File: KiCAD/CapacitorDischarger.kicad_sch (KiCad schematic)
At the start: 47 parts, among them J1 SLB4-G-21, J2 SLB4-G-22, J3 MKDS5/2-9.5, J4 MKDS5/2-9.5, J5 PM-128 input, Q1 MPSA42, Q2 STP10NK80Z

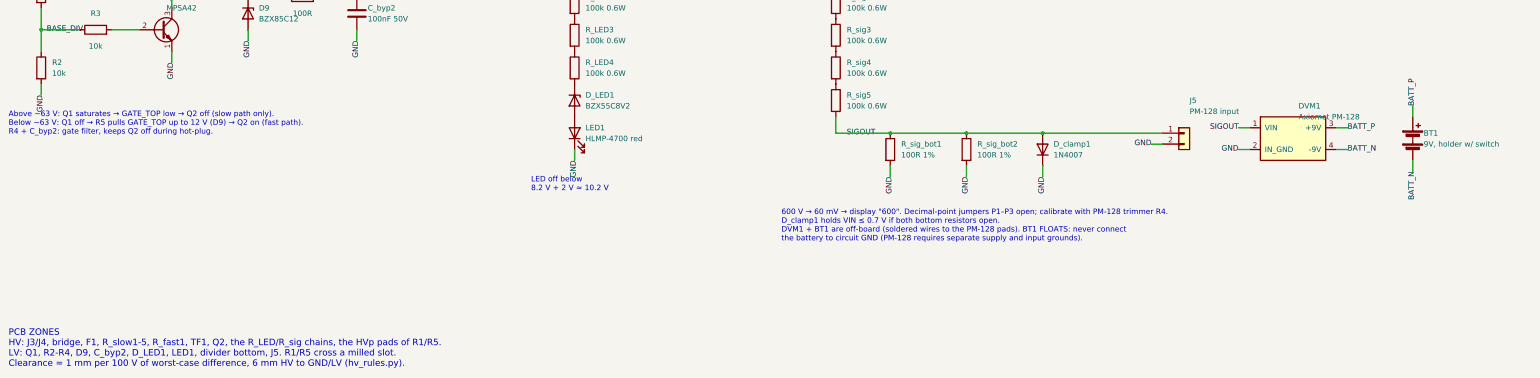
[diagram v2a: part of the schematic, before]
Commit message: Enclosure, front-panel LED via XH, DC-jack 9 V supply, build instructions
- mechanical/enclosure: parametric FreeCAD case for the single-sided board
  (base + screwed cover, PM-128 in the cover, sockets in line with J3/J4,
  9 V jack on the left wall with a floating-supply warning, LED on the front,
  baffled vents, snap hooks + supports for the 2-hole PCB), fit-check script
- LED1 off-board on a JST XH cable (J6); D_clamp2 (BZX55C8V2) holds LED_A at
  8.2 V if the LED is unplugged; sims 15/15 PASS; both boards re-placed, DRC clean
- PM-128 powered from any floating 9 V via a panel DC jack (battery box dropped)
- instruction.md: PCB making, assembly, wiring, tests, calibration, use

Co-Authored-By: Claude Opus 5.5 (1M context) <noreply@anthropic.com>
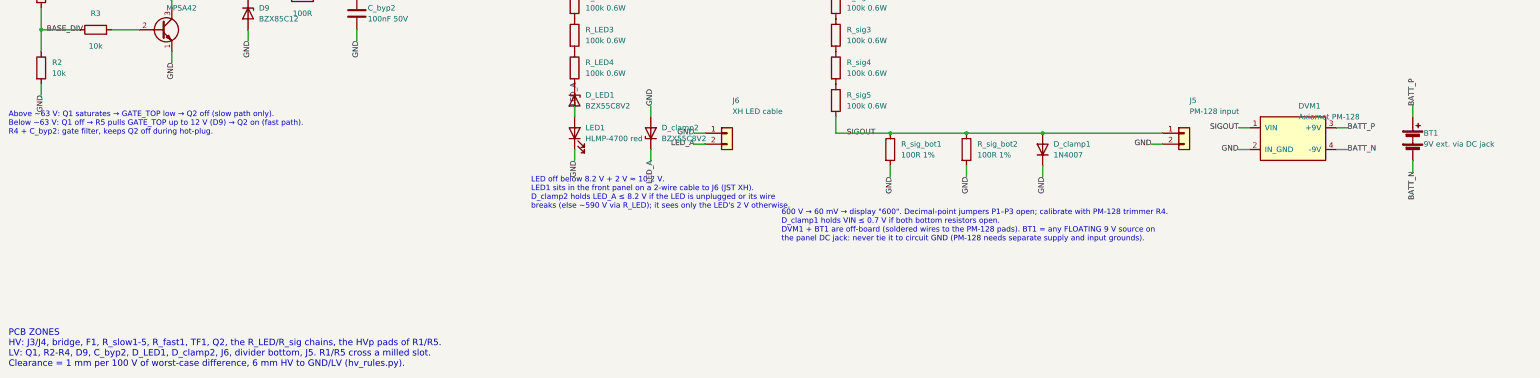
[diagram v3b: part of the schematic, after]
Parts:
- added D_clamp2: BZX55C8V2, Diode_THT:D_DO-35_SOD27_P5.08mm_Vertical_AnodeUp, symbol Device:D_Zener
- added J6: XH LED cable, Connector_JST:JST_XH_B2B-XH-A_1x02_P2.50mm_Vertical, symbol Connector_Generic:Conn_01x02
- BT1: value 9V, holder w/ switch -> 9V ext. via DC jack; MPN Westinghouse 6LR61 + 9 V battery box with ON/OFF switch (bo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 -> Mufa DC mama 5.5x2.1 (ComponentsDB comp_231, same jack as S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
- LED1: footprint LED_THT:LED_D5.0mm -> (none)
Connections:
- net GND: now also D_clamp2.2 (A), J6.1 (Pin_1)
- net LED_A: now reaches D_LED1.2 (A), LED1.2 (A)
- net LED_A: now also D_clamp2.1 (K), J6.2 (Pin_2)
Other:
- note added: "600 V → 60 mV → display "600". Decimal-point jumpers P1–P3 open; calibrate with PM-128 trimmer R4. D_clamp1 holds VIN ≤ 0.7 V if both bottom resistors open. DVM1 + BT1 are off-board (soldered wires to the PM-128 pads). BT1 = any FLOATING 9 V source on the panel DC jack: never tie it to circuit GND (PM-128 needs separate supply and input grounds)."
- note added: "LED off below 8.2 V + 2 V ≈ 10.2 V. LED1 sits in the front panel on a 2-wire cable to J6 (JST XH). D_clamp2 holds LED_A ≤ 8.2 V if the LED is unplugged or its wire breaks (else ~590 V via R_LED); it sees only the LED's 2 V otherwise."
- note added: "PCB ZONES HV: J3/J4, bridge, F1, R_slow1-5, R_fast1, TF1, Q2, the R_LED/R_sig chains, the HVp pads of R1/R5. LV: Q1, R2-R4, D9, C_byp2, D_LED1, D_clamp2, J6, divider bottom, J5. R1/R5 cross a milled slot. Clearance = 1 mm per 100 V of worst-case difference, 6 mm HV to GND/LV (hv_rules.py)."
- note removed: "600 V → 60 mV → display "600". Decimal-point jumpers P1–P3 open; calibrate with PM-128 trimmer R4. D_clamp1 holds VIN ≤ 0.7 V if both bottom resistors open. DVM1 + BT1 are off-board (soldered wires to the PM-128 pads). BT1 FLOATS: never connect the battery to circuit GND (PM-128 requires separate supply and input grounds)."
- note removed: "LED off below 8.2 V + 2 V ≈ 10.2 V"
- note removed: "PCB ZONES HV: J3/J4, bridge, F1, R_slow1-5, R_fast1, TF1, Q2, the R_LED/R_sig chains, the HVp pads of R1/R5. LV: Q1, R2-R4, D9, C_byp2, D_LED1, LED1, divider bottom, J5. R1/R5 cross a milled slot. Clearance = 1 mm per 100 V of worst-case difference, 6 mm HV to GND/LV (hv_rules.py)."
